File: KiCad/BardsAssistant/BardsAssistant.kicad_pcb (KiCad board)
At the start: 2 copper layers, 100 x 100 mm, 75 parts, among them IC1 ESP32-S3-MINI-1-N8, J1 USB_C_Receptacle_USB2.0_16P, J2 Conn_01x24, J3 JST-PH-2-SMT-RA, Q1 Si1308EDL, Q3 AO3401A, SW1 SW_Push, SW2 SW_Push, SW3 SW_Push, SW4 SW_Push, SW5 SW_Push, SW6 SW_Push, U1 TPS63001, U2 USBLC6-2SC6, U3 MCP73831/2

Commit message: updated pcb v1
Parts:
- removed TP6: TestPoint, TestPoint:TestPoint_Pad_2.0x2.0mm
- added G***: LOGO, LOGO, B.Cu at (151.4, 104.8)
- C1, C10, C11, C12, C13, C15, C16, C17, C18, C19, C2, C20, C21, C22, C3, C4, C5, C6, C7, C8, C9, D1, D2, D3, D4, D5, D6, D7, D8, D9, F1, FB1, IC1, J1, J2, J3, L1, L2, Q1, Q3, R1, R10, R11, R12, R13, R14, R15, R16, R17, R2, R3, R4, R5, R6, R7, R8, R9, SW1, SW2, SW3, SW4, SW5, SW6, TP1, TP2, TP3, U1, U2, U3: moved to B.Cu
- TP5: value TestPoint -> GND; moved to B.Cu
- moved C21 96.5 mm to (104.0, 153.2)
- moved U3 91.9 mm to (108.8, 149.8)
- moved C22 84.2 mm to (113.4, 148.0)
- moved J3 68.2 mm to (107.2, 142.8), turned to 90 degrees
- moved U1 66.8 mm to (112.9, 121.5)
- moved D9 63.9 mm to (113.8, 138.0), turned to 180 degrees
- moved D4 62.5 mm to (166.5, 67.5), turned to -90 degrees
- moved U2 61.3 mm to (115.8, 106.3)
- moved R10 60.8 mm to (113.0, 150.0)
- moved TP5 58.6 mm to (178.9, 68.6)
- moved R13 57.1 mm to (113.5, 135.2)
- moved SW6 56.5 mm to (105.3, 59.2), turned to -90 degrees
- moved R3 56.1 mm to (139.0, 60.5), turned to 180 degrees
- moved Q3 55.4 mm to (123.2, 129.3), turned to -90 degrees
- moved D3 54.5 mm to (132.0, 65.7), turned to 90 degrees
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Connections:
- C10 pad 2: VDD33 -> +3V3
- D1 pad 4: +3.3V -> +3V3
- IC1 pad 33: unconnected-(IC1-IO37-Pad33) -> Net-(IC1-IO37)
- IC1 pad 34: unconnected-(IC1-IO38-Pad34) -> Net-(IC1-IO38)
- IC1 pad 5: /TP8 -> unconnected-(IC1-IO1-Pad5)
- IC1 pad 6: /TP9 -> unconnected-(IC1-IO2-Pad6)
- L1 pad 1: VDD33 -> +3V3
- TP8 pad 1: /TP8 -> Net-(IC1-IO37)
- TP9 pad 1: /TP9 -> Net-(IC1-IO38)
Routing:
- net GND: track 0.00 -> 108.6 mm, vias 0 -> 50
- net /RST: track 0.00 -> 75.8 mm, vias 0 -> 3
- net /BUSY: track 0.00 -> 75.4 mm
- net /D+: track 0.00 -> 74.4 mm
- net /D-: track 0.00 -> 72.6 mm
- net /USB_5V: track 0.00 -> 71.9 mm, vias 0 -> 2
- net /SCK: track 0.00 -> 70.1 mm, vias 0 -> 2
- net /MOSI: track 0.00 -> 67.0 mm, vias 0 -> 2
- net /CS: track 0.00 -> 66.6 mm, vias 0 -> 2
- net /DC: track 0.00 -> 61.1 mm, vias 0 -> 2
- net Net-(IC1-IO7): track 0.00 -> 57.0 mm, vias 0 -> 2
- net /BAT: track 0.00 -> 46.9 mm
- net Net-(IC1-IO6): track 0.00 -> 46.5 mm, vias 0 -> 2
- net /SYS: track 0.00 -> 38.7 mm
- net Net-(IC1-IO5): track 0.00 -> 38.1 mm, vias 0 -> 2
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- added copper zone on In2.Cu, net +3V3
- added copper zone on In1.Cu, net GND
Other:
- copper layers 2 -> 4
- board text added: "330Ω"
- board text added: "3V3"
- board text added: "4.7uF"
- board text added: "5V"
- board text added: "BAT"
- board text added: "BOOT"
- board text added: "Bard's Assistant V1"
- board text added: "C3"
- board text added: "GND"
- board text added: "NEXT"
- board text added: "PREV"
- board text added: "R10"
- board text added: "RANDOM"
- board text added: "RESET"
- board text added: "SLEEP"
- board text added: "SYS"
- board text added: "U2"
- board text removed: "Approx screen hat size. thinking about putting on bottom of pcb"

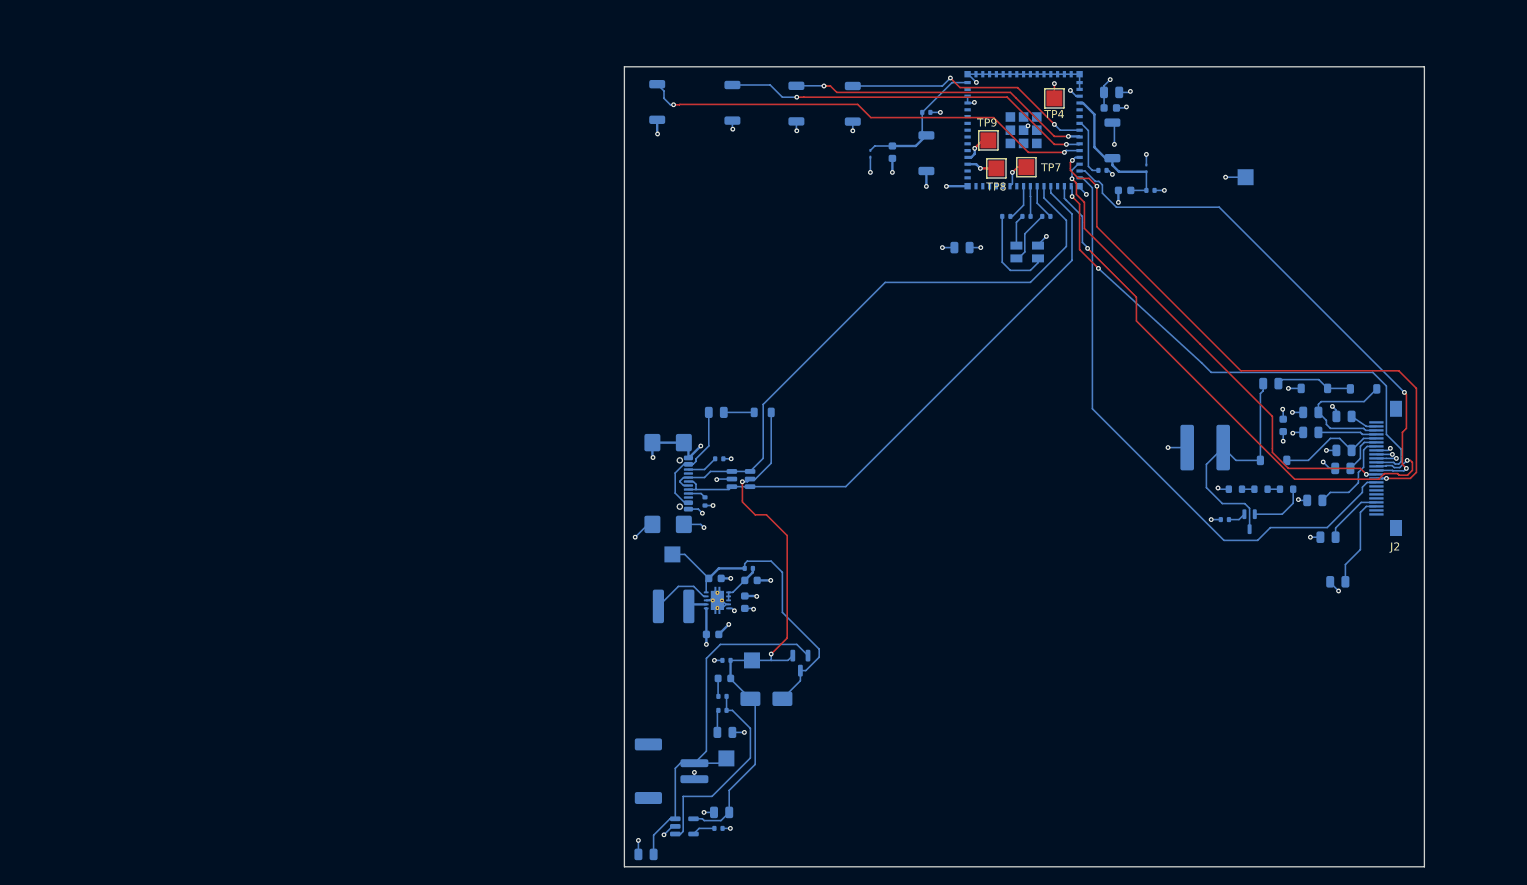
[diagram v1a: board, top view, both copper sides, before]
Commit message: Update KiCad schematic, PCB, and library files
- Update schematic and PCB layout
- Add LED-SMD-SM1210RGB footprint to BardAssLibrary
- Remove old Gerber exports and production files, update with new
- Remove BAV1.zip
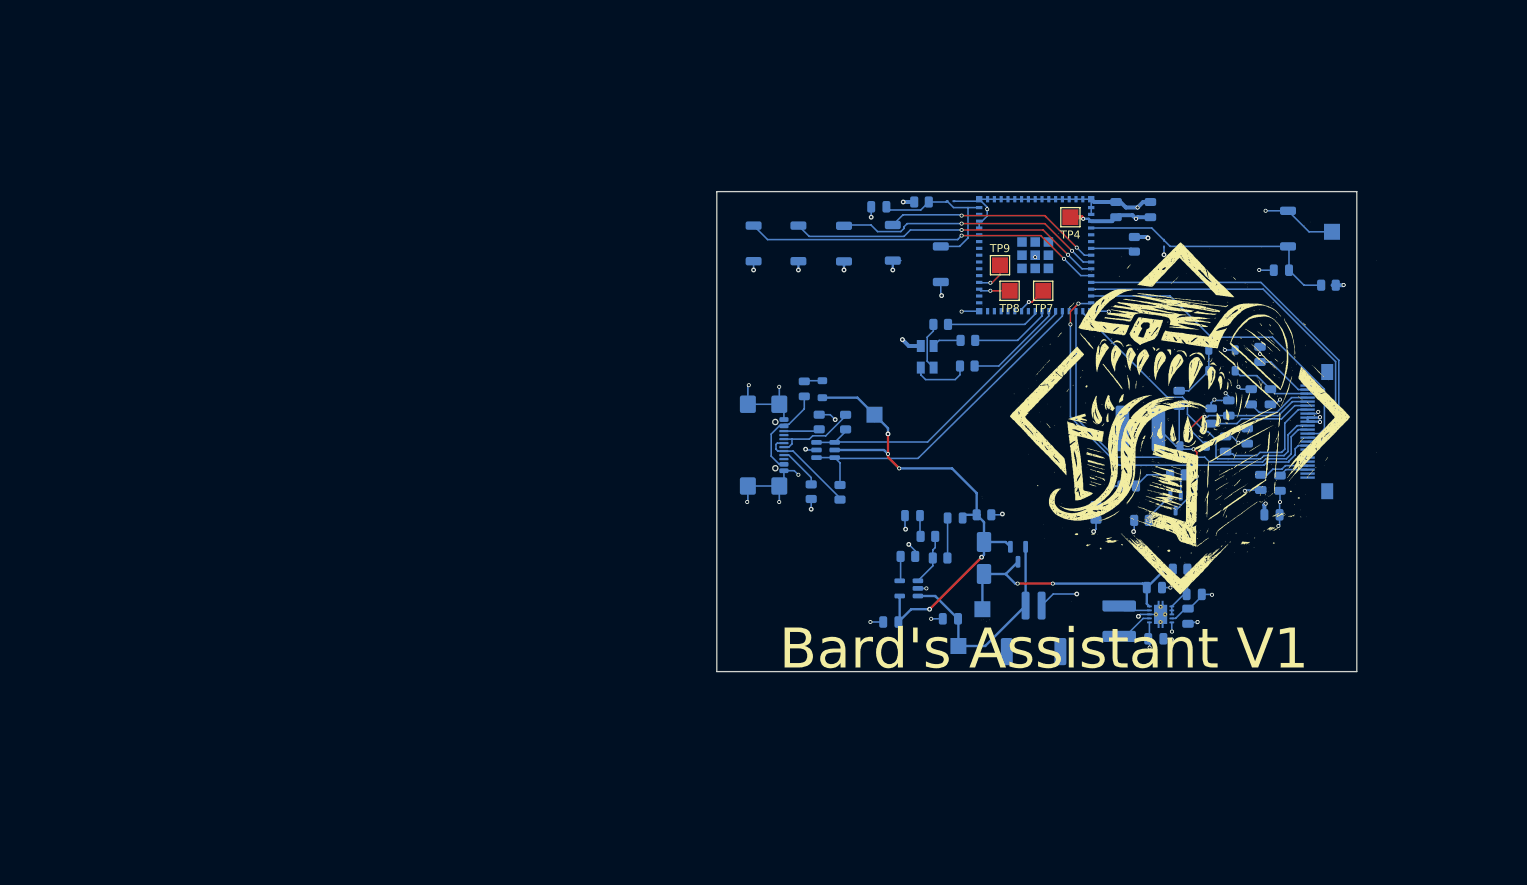
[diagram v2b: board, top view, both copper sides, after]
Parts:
- added R18: 22R, Resistor_SMD:R_0805_2012Metric, B.Cu at (128.2, 108.0)
- added R19: 22R, Resistor_SMD:R_0805_2012Metric, B.Cu at (128.9, 99.2)
- C1, C13, C2, C4, C5, C6, C7, C8: footprint Capacitor_SMD:C_0603_1608Metric -> Capacitor_SMD:C_0805_2012Metric
- D1: value XL-3227RGB-RF -> SM1210RGB
- D5: footprint LED_SMD:LED_0603_1608Metric -> LED_SMD:LED_0805_2012Metric
- G***: moved to F.Cu
- R1, R11, R12, R13, R14, R15, R16, R2, R3, R5, R6, R7, R8: footprint Resistor_SMD:R_0402_1005Metric -> Resistor_SMD:R_0805_2012Metric
- R10: value 5K -> 5K1; footprint Resistor_SMD:R_0402_1005Metric -> Resistor_SMD:R_0805_2012Metric
- R17, R4, R9: footprint Resistor_SMD:R_0603_1608Metric -> Resistor_SMD:R_0805_2012Metric
- moved L2 55.7 mm to (163.1, 124.1), turned to -90 degrees
- moved U1 55.4 mm to (168.3, 123.2)
- moved C2 55.4 mm to (172.5, 120.8)
- moved C6 55.4 mm to (171.7, 123.5)
- moved C5 55.4 mm to (167.7, 126.3)
- moved C1 54.9 mm to (167.5, 119.9)
- moved R15 53.9 mm to (170.7, 117.6)
- moved C10 51.2 mm to (182.2, 110.8), turned to 180 degrees
- moved J3 48.6 mm to (152.4, 125.0), turned to 180 degrees
- moved C21 48.1 mm to (142.0, 123.8)
- moved R10 41.4 mm to (136.7, 116.0)
- moved U3 40.9 mm to (136.8, 120.0), turned to 180 degrees
- moved TP3 39.4 mm to (146.0, 122.6)
- moved R6 37.0 mm to (146.2, 110.8), turned to 180 degrees
- moved D9 35.8 mm to (137.3, 110.9), turned to 0 degrees
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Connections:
- D1 pad 1: Net-(D1-RK) -> +3V3
- D1 pad 2: Net-(D1-GK) -> Net-(D1-RK)
- D1 pad 3: Net-(D1-BK) -> Net-(D1-GK)
- D1 pad 4: +3V3 -> Net-(D1-BK)
- J1 pad A6: /D+ -> Net-(J1-D+-PadA6)
- J1 pad A7: /D- -> Net-(J1-D--PadA7)
- J1 pad B6: /D+ -> Net-(J1-D+-PadA6)
- J1 pad B7: /D- -> Net-(J1-D--PadA7)
- R11 pad 2: Net-(IC1-IO17) -> Net-(IC1-IO18)
- R14 pad 2: Net-(IC1-IO18) -> Net-(IC1-IO17)
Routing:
- net /D+: track 74.4 -> 39.4 mm
- net /D-: track 72.6 -> 42.7 mm
- net /RST: track 75.8 -> 47.7 mm, vias 3 -> 0
- net /MOSI: track 67.0 -> 41.0 mm, vias 2 -> 0
- net /BUSY: track 75.4 -> 49.9 mm, vias 0 -> 2
- net /CS: track 66.6 -> 41.3 mm, vias 2 -> 0
- net GND: track 108.6 -> 133.4 mm, vias 50 -> 46
- net /SCK: track 70.1 -> 47.5 mm, vias 2 -> 0
- net /BAT: track 46.9 -> 27.5 mm
- net Net-(U3-STAT): track 25.2 -> 6.45 mm
- net /DC: track 61.1 -> 46.2 mm, vias 2 -> 0
- net Net-(D4-A2): track 19.1 -> 34.0 mm
- net Net-(J1-D--PadA7): track 0.00 -> 12.4 mm
- net Net-(IC1-IO7): track 57.0 -> 45.5 mm
- net Net-(J1-D+-PadA6): track 0.00 -> 10.9 mm
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- added copper zone on In1.Cu, net +3V3
- added copper zone on In2.Cu, net GND
- removed copper zone on In2.Cu, net +3V3
- removed copper zone on In1.Cu, net GND
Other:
- board size 100 x 100 mm -> 80 x 60 mm
- board text added: "ENABLE"
- board text added: "ESP32-S3"
- board text added: "USB 5V"
- board text removed: "330Ω"
- board text removed: "3V3"
- board text removed: "4.7uF"
- board text removed: "5V"
- board text removed: "BOOT"
- board text removed: "C3"
- board text removed: "R10"
- board text removed: "U2"
